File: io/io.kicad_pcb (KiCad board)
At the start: 4 copper layers, 84 x 40 mm, 48 parts, among them J2 Conn_02x03, J3 QwST, J4 SM03B-SRSS-TB, J5 QwST, J6 Conn_02x08_Odd_Even, SW1 SW_Push, SW2 SW_Push, U1 RP2350_80QFN, U2 74LVC32, U3 W25Q32JVS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

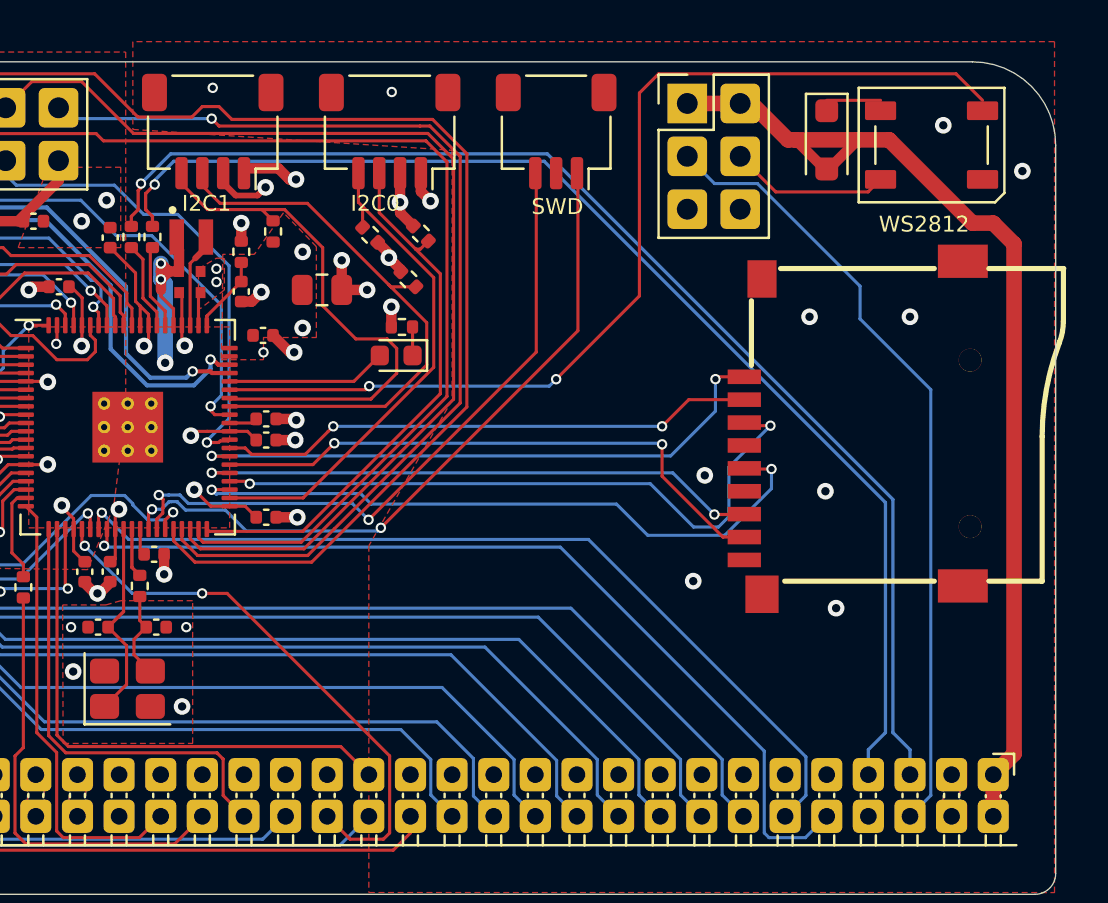
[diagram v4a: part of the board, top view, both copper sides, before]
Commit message: CPU and IO production fixes
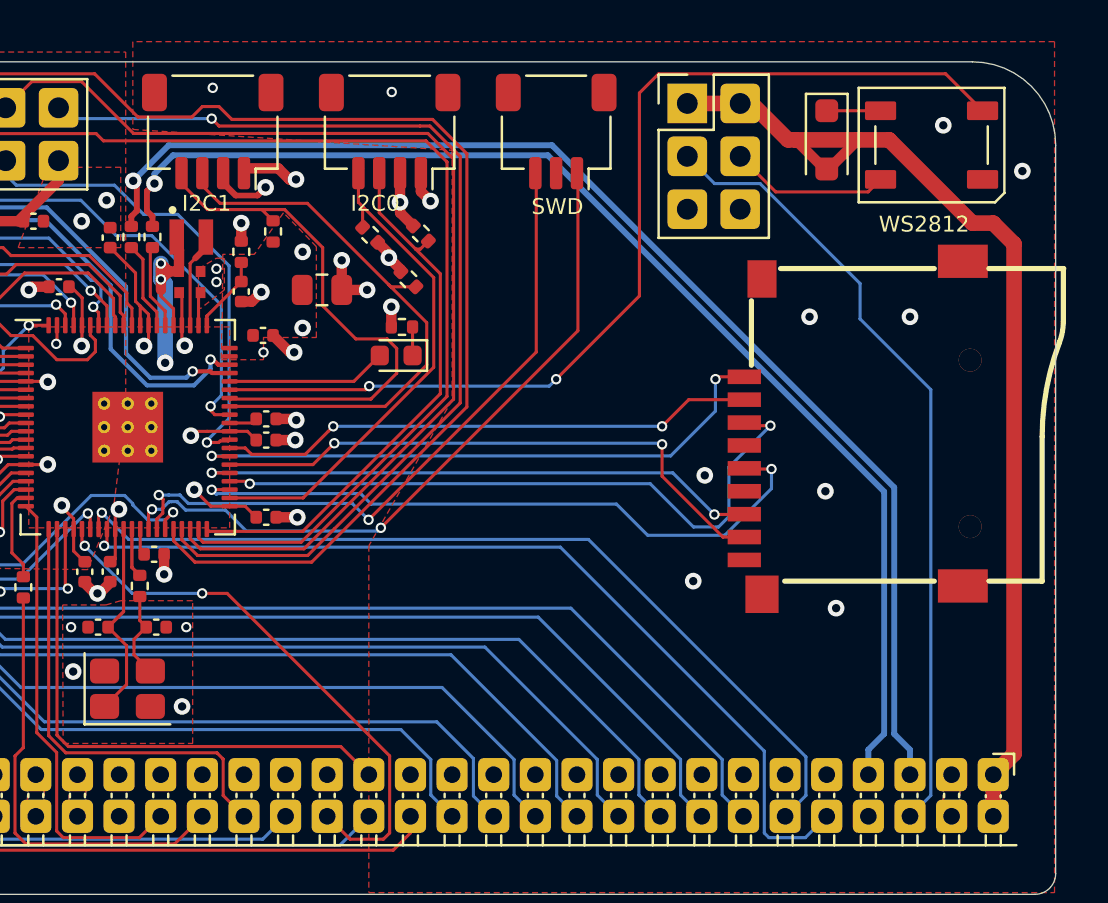
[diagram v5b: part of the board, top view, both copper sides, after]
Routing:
- net /USB_D+: track 59.4 -> 60.6 mm
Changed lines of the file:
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@@
 			)
 		)
-		(property "JLC" "C132988"
+		(property "JLC" "C2867091"
 			(at 0 0 90)
 			(unlocked yes)
@@
 			)
 		)
-		(property "JLC" "C3410"
+		(property "JLC" "C3407"
 			(at 0 0 0)
 			(unlocked yes)
@@
 			)
 		)
+		(property "JLC" "C179173"
+			(at 0 0 0)
+			(unlocked yes)
+			(layer "F.Fab")
+			(hide yes)
+			(effects
+				(font
+					(size 1 1)
+					(thickness 0.15)
+				)
+			)
+		)
 		(property ki_fp_filters "SOIC*5.23x5.23mm*P1.27mm*")
 		(sheetname "/")
@@
 			)
 		)
+		(property "JLC" "C42415655"
+			(at 0 0 0)
+			(unlocked yes)
+			(layer "F.Fab")
+			(hide yes)
+			(effects
+				(font
+					(size 1 1)
+					(thickness 0.15)
+				)
+			)
+		)
 		(sheetname "/")
 		(sheetfile "io.kicad_sch")
@@
 	)
 	(segment
-		(start 167.5864 83.6)
-		(end 165 83.6)
+		(start 167.5864 84.1)
+		(end 165 84.1)
 		(width 0.15)
 		(layer "F.Cu")
@@
 	)
 	(segment
-		(start 156 93)
-		(end 156 83.693)
+		(start 172.4864 84.1)
+		(end 170.7124 82.326)
 		(width 0.15)
 		(layer "F.Cu")
@@
 	)
 	(segment
-		(start 156 83.25)
+		(start 156 93)
 		(end 156 83.693)
 		(width 0.15)
@@
 	)
 	(segment
-		(start 143.018 97.3328)
-		(end 142.8468 97.504)
+		(start 156 83.25)
+		(end 156 83.693)
 		(width 0.15)
 		(layer "F.Cu")
@@
 	)
 	(segment
-		(start 172.4864 83.6)
-		(end 171.2124 82.326)
+		(start 143.018 97.3328)
+		(end 142.8468 97.504)
 		(width 0.15)
 		(layer "F.Cu")
@@
 	)
 	(segment
-		(start 171.2124 82.326)
+		(start 170.7124 82.326)
 		(end 156.924 82.326)
 		(width 0.15)
@@
 	)
 	(segment
-		(start 132.27475 88.848749)
-		(end 132.27475 88.082357)
-		(width 0.1575)
+		(start 132.338 88.911999)
+		(end 132.338 87.962)
+		(width 0.284)
 		(layer "F.Cu")
 		(net 33)
 	)
 	(segment
-		(start 132.27475 88.082357)
-		(end 132.711833 87.645274)
-		(width 0.1575)
+		(start 132.604 89.658)
+		(end 132.604 89.177999)
+		(width 0.284)
 		(layer "F.Cu")
 		(net 33)
@@
 	(segment
 		(start 132.604 89.177999)
-		(end 132.27475 88.848749)
-		(width 0.1575)
+		(end 132.338 88.911999)
+		(width 0.284)
 		(layer "F.Cu")
 		(net 33)
 	)
 	(segment
-		(start 132.604 89.658)
-		(end 132.604 89.177999)
-		(width 0.1575)
+		(start 132.338 87.962)
+		(end 132.7 87.6)
+		(width 0.284)
 		(layer "F.Cu")
 		(net 33)
 	)
 	(via
-		(at 132.711833 87.645274)
-		(size 0.5)
-		(drill 0.3)
+		(at 132.7 87.6)
+		(size 0.8)
+		(drill 0.4)
 		(layers "F.Cu" "B.Cu")
-		(free yes)
 		(net 33)
 	)
@@
 		(start 167 114.799999)
 		(end 167 116)
-		(width 0.1575)
-		(layer "B.Cu")
-		(net 33)
-	)
-	(segment
-		(start 167.82125 102.924042)
-		(end 167.82125 113.978749)
-		(width 0.1575)
+		(width 0.284)
 		(layer "B.Cu")
 		(net 33)
 	)
 	(segment
-		(start 132.711833 87.645274)
-		(end 132.711833 87.504088)
-		(width 0.2)
+		(start 133.590434 86.242)
+		(end 151.59976 86.242)
+		(width 0.284)
 		(layer "B.Cu")
 		(net 33)
 	)
 	(segment
-		(start 132.711833 87.645274)
-		(end 132.711833 87.443749)
-		(width 0.1575)
+		(start 132.7 87.132434)
+		(end 133.590434 86.242)
+		(width 0.284)
 		(layer "B.Cu")
 		(net 33)
 	)
 	(segment
-		(start 151.425958 86.52875)
-		(end 167.82125 102.924042)
-		(width 0.1575)
+		(start 167.758 102.40024)
+		(end 167.758 114.041999)
+		(width 0.284)
 		(layer "B.Cu")
 		(net 33)
 	)
 	(segment
-		(start 132.711833 87.443749)
-		(end 133.626832 86.52875)
-		(width 0.1575)
+		(start 167.758 114.041999)
+		(end 167 114.799999)
+		(width 0.284)
 		(layer "B.Cu")
 		(net 33)
 	)
 	(segment
-		(start 167.82125 113.978749)
-		(end 167 114.799999)
-		(width 0.1575)
+		(start 151.59976 86.242)
+		(end 167.758 102.40024)
+		(width 0.284)
 		(layer "B.Cu")
 		(net 33)
 	)
 	(segment
-		(start 133.626832 86.52875)
-		(end 151.425958 86.52875)
-		(width 0.1575)
+		(start 132.7 87.6)
+		(end 132.7 87.132434)
+		(width 0.284)
 		(layer "B.Cu")
 		(net 33)
@@
 	)
 	(segment
-		(start 131.91725 87.934275)
-		(end 132.05 87.801525)
-		(width 0.1575)
+		(start 131.854 88.911999)
+		(end 131.854 87.645228)
+		(width 0.284)
 		(layer "F.Cu")
 		(net 55)
@@
 		(start 131.588 89.658)
 		(end 131.588 89.177999)
-		(width 0.1575)
-		(layer "F.Cu")
-		(net 55)
-	)
-	(segment
-		(start 132.05 87.801525)
-		(end 132.05 87.6)
-		(width 0.1575)
+		(width 0.284)
 		(layer "F.Cu")
 		(net 55)
@@
 	(segment
 		(start 131.588 89.177999)
-		(end 131.91725 88.848749)
-		(width 0.1575)
+		(end 131.854 88.911999)
+		(width 0.284)
 		(layer "F.Cu")
 		(net 55)
 	)
 	(segment
-		(start 131.91725 88.848749)
-		(end 131.91725 87.934275)
-		(width 0.1575)
+		(start 131.854 87.645228)
+		(end 131.678363 87.469591)
+		(width 0.284)
 		(layer "F.Cu")
 		(net 55)
 	)
 	(via
-		(at 132.05 87.6)
-		(size 0.5)
-		(drill 0.3)
+		(at 131.678363 87.469591)
+		(size 0.8)
+		(drill 0.4)
 		(layers "F.Cu" "B.Cu")
-		(free yes)
 		(net 55)
 	)
 	(segment
-		(start 169 114.799999)
-		(end 169 116)
-		(width 0.1575)
+		(start 168.242 114.041999)
+		(end 169 114.799999)
+		(width 0.284)
 		(layer "B.Cu")
 		(net 55)
 	)
 	(segment
-		(start 133.47875 86.17125)
-		(end 151.574042 86.17125)
-		(width 0.1575)
+		(start 131.678363 87.469591)
+		(end 133.389954 85.758)
+		(width 0.284)
 		(layer "B.Cu")
 		(net 55)
 	)
 	(segment
-		(start 168.17875 113.978749)
-		(end 169 114.799999)
-		(width 0.1575)
+		(start 169 114.799999)
+		(end 169 116)
+		(width 0.284)
 		(layer "B.Cu")
 		(net 55)
 	)
 	(segment
-		(start 151.574042 86.17125)
-		(end 168.17875 102.775958)
-		(width 0.1575)
+		(start 168.242 102.19976)
+		(end 168.242 114.041999)
+		(width 0.284)
 		(layer "B.Cu")
 		(net 55)
 	)
 	(segment
-		(start 168.17875 102.775958)
-		(end 168.17875 113.978749)
-		(width 0.1575)
+		(start 133.389954 85.758)
+		(end 151.80024 85.758)
+		(width 0.284)
 		(layer "B.Cu")
 		(net 55)
 	)
 	(segment
-		(start 132.05 87.6)
-		(end 133.47875 86.17125)
-		(width 0.1575)
+		(start 151.80024 85.758)
+		(end 168.242 102.19976)
+		(width 0.284)
 		(layer "B.Cu")
 		(net 55)
@@
 	)
 	(segment
-		(start 166.6 92.529492)
-		(end 161.670508 87.6)
+		(start 166.6 92.4)
+		(end 161.8 87.6)
 		(width 0.15)
 		(layer "B.Cu")
@@
 	)
 	(segment
-		(start 166.6 94.1)
-		(end 166.6 92.529492)
+		(start 170 97.5)
+		(end 166.6 94.1)
 		(width 0.15)
 		(layer "B.Cu")
@@
 	)
 	(segment
-		(start 161.670508 87.6)
-		(end 159.61 87.6)
+		(start 166.6 94.1)
+		(end 166.6 92.4)
 		(width 0.15)
 		(layer "B.Cu")
@@
 	)
 	(segment
-		(start 170 97.5)
-		(end 166.6 94.1)
+		(start 170 117)
+		(end 170 97.5)
 		(width 0.15)
 		(layer "B.Cu")
@@
 	)
 	(segment
-		(start 170 117)
-		(end 170 97.5)
+		(start 161.8 87.6)
+		(end 159.61 87.6)
 		(width 0.15)
 		(layer "B.Cu")
@@
 		(polygon
 			(pts
-				(xy 84.582 121.666) (xy 186.944 121.666) (xy 186.944 81.28) (xy 84.582 81.28)
+				(xy 91.582 121.666) (xy 175.944 121.666) (xy 175.944 81.28) (xy 91.582 81.28)
 			)
 		)
@@
 		(polygon
 			(pts
-				(xy 84.582 121.666) (xy 186.944 121.666) (xy 186.944 81.28) (xy 84.582 81.28)
+				(xy 91.582 121.666) (xy 175.944 121.666) (xy 175.944 81.28) (xy 91.582 81.28)
 			)
 		)

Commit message: Add backplane
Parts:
- R5: value 27 -> 33
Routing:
- net GND: track 25.0 -> 29.7 mm, vias 44 -> 47

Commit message: RAM board attempt 2
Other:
- board text added: "RV2048 IO v0.1 © Michael Bell 2026 JLCJLCJLCJLC"
- board text removed: "RV2048 CPU v0.1 © Mike Bell 2026 JLCJLCJLCJLC"
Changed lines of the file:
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@@
 		)
 	)
-	(gr_text "RV2048 CPU v0.1\n© Mike Bell 2026\nJLCJLCJLCJLC"
+	(gr_text "RV2048 IO v0.1\n© Michael Bell 2026\nJLCJLCJLCJLC"
 		(at 175 101.75 90)
 		(layer "B.SilkS")

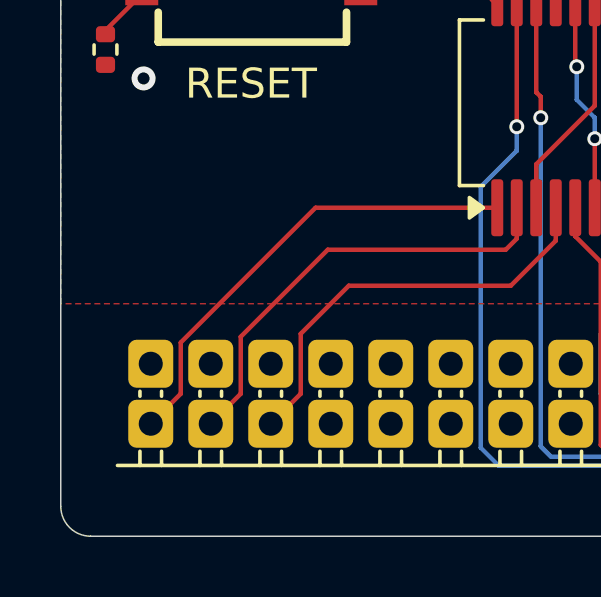
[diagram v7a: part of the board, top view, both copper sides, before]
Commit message: Backplane reset and fixes
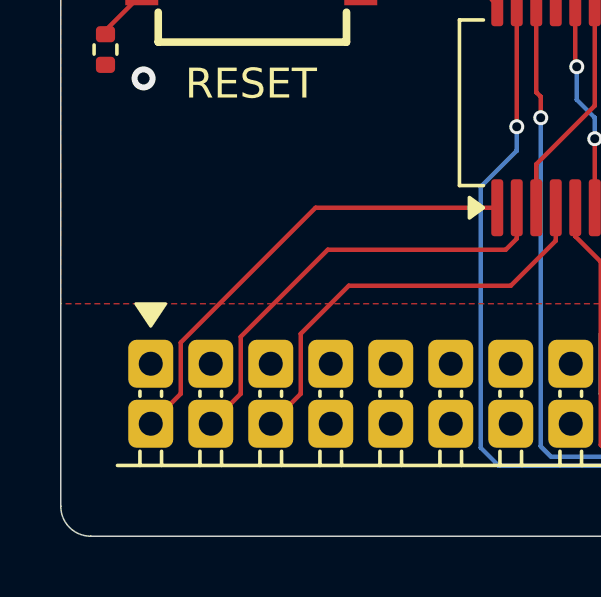
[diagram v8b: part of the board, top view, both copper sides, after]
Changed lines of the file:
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@@
+			(layer "F.SilkS")
+		)
+		(fp_poly
+			(pts
+				(xy -39.5 -3.5) (xy -39 -2.75) (xy -38.5 -3.5)
+			)
+			(stroke
+				(width 0.1)
+				(type solid)
+			)
+			(fill yes)
 			(layer "F.SilkS")
 		)
